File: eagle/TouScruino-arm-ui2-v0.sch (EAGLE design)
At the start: 45 parts, among them IC1 LMV321M5, Q2 MMBT2222A, U3 MIC5209-3.3YS, U4 MCP73831

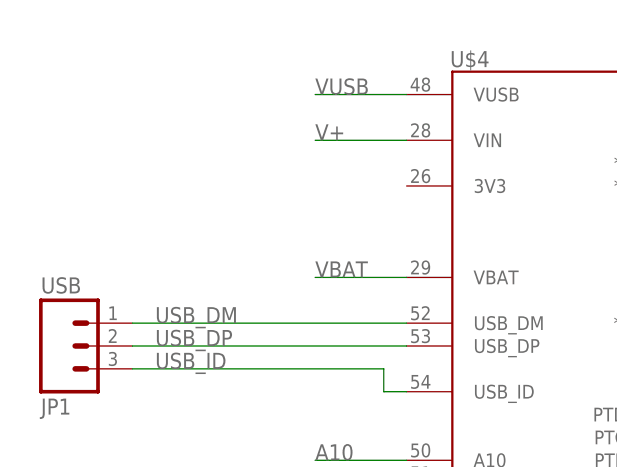
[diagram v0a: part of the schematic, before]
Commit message: 
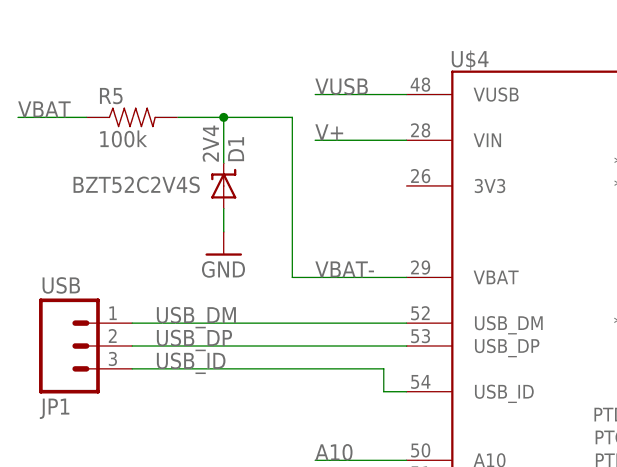
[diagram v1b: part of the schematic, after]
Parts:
- added D1: 2V4, SparkFun:DIODE-ZENER-BZT52
- added R5: 100k, SparkFun:RESISTOR0805-RES
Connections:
- new net VBAT-: D1.C, R5.2, U$4.VBAT
- net GND: now also D1.A
- net VBAT: now also R5.1; no longer U$4.VBAT
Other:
- note added: "BZT52C2V4S"
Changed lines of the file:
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@@
 <part name="GND11" library="SparkFun" deviceset="GND" device=""/>
 <part name="JP8" library="wibauxl" deviceset="M01" device="SMD" value="CHARGE"/>
+<part name="D1" library="SparkFun" deviceset="DIODE-ZENER" device="-BZT52" value="2V4"/>
+<part name="R5" library="SparkFun" deviceset="RESISTOR" device="0805-RES" value="100k"/>
+<part name="GND14" library="SparkFun" deviceset="GND" device=""/>
 </parts>
 <sheets>
@@
 <text x="177.8" y="60.96" size="1.778" layer="94">Use jumper (or solder joint) to choose
 buffered DAC or A14 on the shield pin</text>
+<text x="27.94" y="158.496" size="1.778" layer="96" rot="R180">BZT52C2V4S</text>
 </plain>
 <instances>
@@
 <instance part="GND11" gate="1" x="182.88" y="22.86" rot="MR0"/>
 <instance part="JP8" gate="G$1" x="48.26" y="-60.96"/>
+<instance part="D1" gate="G$1" x="30.48" y="157.48" rot="MR90"/>
+<instance part="R5" gate="G$1" x="20.32" y="165.1"/>
+<instance part="GND14" gate="1" x="30.48" y="149.86"/>
 </instances>
 <busses>
@@
 <wire x1="182.88" y1="27.94" x2="182.88" y2="25.4" width="0.1524" layer="91"/>
 </segment>
+<segment>
+<pinref part="D1" gate="G$1" pin="A"/>
+<pinref part="GND14" gate="1" pin="GND"/>
+<wire x1="30.48" y1="154.94" x2="30.48" y2="152.4" width="0.1524" layer="91"/>
+</segment>
 </net>
 <net name="AREF" class="0">
@@
 </segment>
 <segment>
-<wire x1="50.8" y1="147.32" x2="40.64" y2="147.32" width="0.1524" layer="91"/>
-<label x="40.64" y="147.32" size="1.778" layer="95"/>
-<pinref part="U$4" gate="G$1" pin="VBAT"/>
+<label x="7.62" y="165.1" size="1.778" layer="95"/>
+<wire x1="15.24" y1="165.1" x2="7.62" y2="165.1" width="0.1524" layer="91"/>
+<pinref part="R5" gate="G$1" pin="1"/>
 </segment>
 </net>
@@
 </segment>
 </net>
+<net name="VBAT-" class="0">
+<segment>
+<wire x1="50.8" y1="147.32" x2="38.1" y2="147.32" width="0.1524" layer="91"/>
+<label x="40.64" y="147.32" size="1.778" layer="95"/>
+<pinref part="U$4" gate="G$1" pin="VBAT"/>
+<pinref part="R5" gate="G$1" pin="2"/>
+<pinref part="D1" gate="G$1" pin="C"/>
+<wire x1="25.4" y1="165.1" x2="30.48" y2="165.1" width="0.1524" layer="91"/>
+<wire x1="30.48" y1="165.1" x2="30.48" y2="160.02" width="0.1524" layer="91"/>
+<wire x1="30.48" y1="165.1" x2="38.1" y2="165.1" width="0.1524" layer="91"/>
+<wire x1="38.1" y1="165.1" x2="38.1" y2="147.32" width="0.1524" layer="91"/>
+<junction x="30.48" y="165.1"/>
+</segment>
+</net>
